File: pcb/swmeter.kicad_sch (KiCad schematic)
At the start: 16 parts, among them J0 Conn_01x02_Female, J1 AudioPlug, J2 Conn_Coaxial, J3 Conn_01x03_Female, J4 Conn_01x03_Female, SW1 SW_SPDT, SW2 SW_SPDT, SW3 SW_DIP_x03, U1 LM3914N

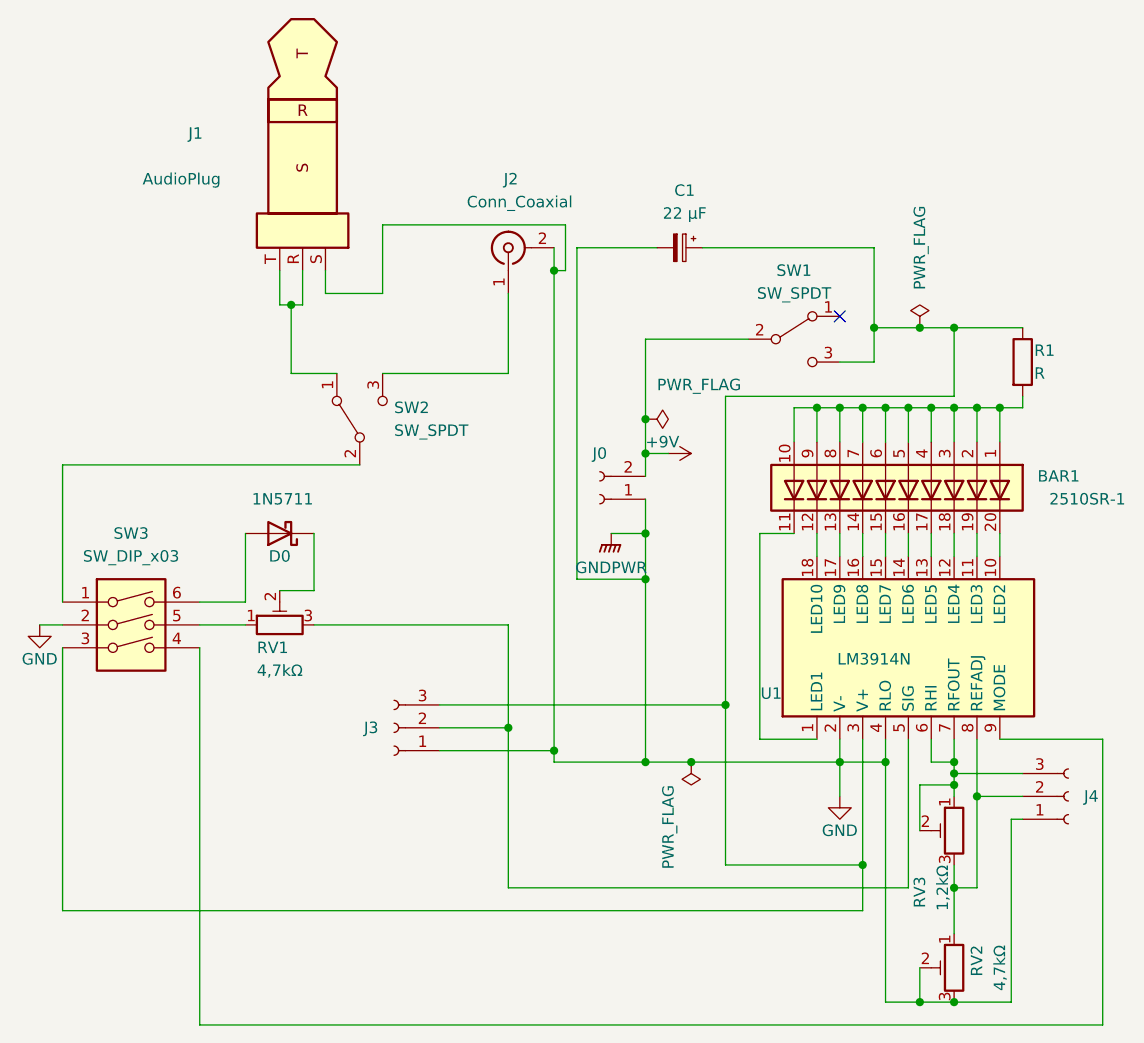
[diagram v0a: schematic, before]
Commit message: add diode for reverse polarity protection
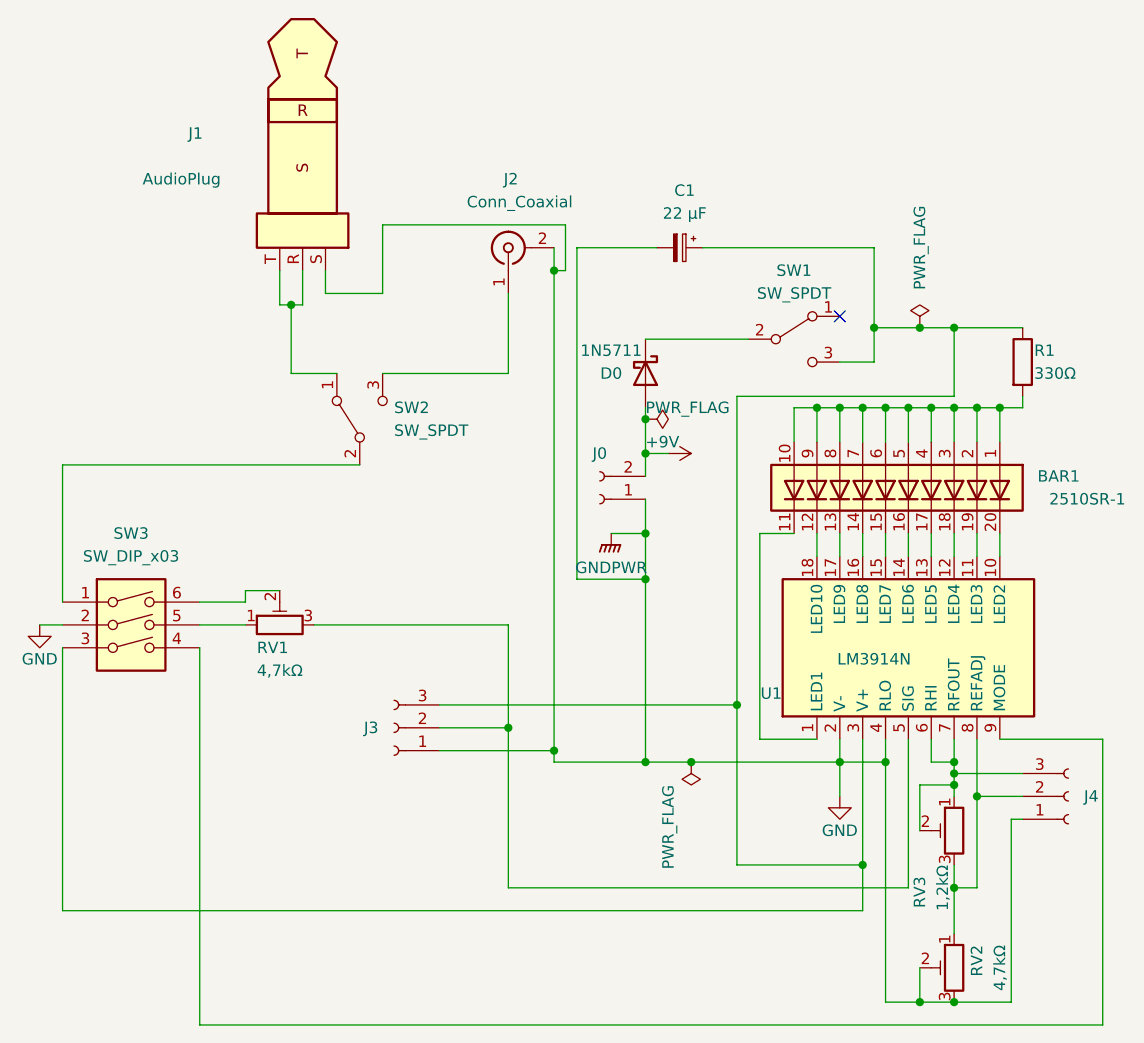
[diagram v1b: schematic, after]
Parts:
- R1: value R -> 330Ω
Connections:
- net +9V: now also D0.2 (A); no longer SW1.2 (B)
- net at SW3.6: now also RV1.2; no longer D0.2 (A)
- net at D0.1 (K): now also SW1.2 (B); no longer RV1.2
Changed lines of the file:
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@@
   (junction (at 250.19 92.71) (diameter 0) (color 0 0 0 0)
   )
+  (junction (at 238.76 125.73) (diameter 0) (color 0 0 0 0)
+  )
   (junction (at 189.23 81.28) (diameter 0) (color 0 0 0 0)
   )
@@
   )
   (junction (at 250.19 132.08) (diameter 0) (color 0 0 0 0)
-  )
-  (junction (at 237.49 125.73) (diameter 0) (color 0 0 0 0)
   )
   (junction (at 265.43 92.71) (diameter 0) (color 0 0 0 0)
@@
     (stroke (width 0) (type default) (color 0 0 0 0))
   )
+  (wire (pts (xy 205.74 125.73) (xy 238.76 125.73))
+    (stroke (width 0) (type default) (color 0 0 0 0))
+  )
   (wire (pts (xy 193.04 80.01) (xy 199.39 80.01))
     (stroke (width 0) (type default) (color 0 0 0 0))
@@
     (stroke (width 0) (type default) (color 0 0 0 0))
   )
+  (wire (pts (xy 184.15 114.3) (xy 184.15 113.03))
+    (stroke (width 0) (type default) (color 0 0 0 0))
+  )
   (wire (pts (xy 219.71 77.47) (xy 218.44 77.47))
     (stroke (width 0) (type default) (color 0 0 0 0))
@@
     (stroke (width 0) (type default) (color 0 0 0 0))
   )
+  (wire (pts (xy 238.76 125.73) (xy 238.76 143.51))
+    (stroke (width 0) (type default) (color 0 0 0 0))
+  )
+  (wire (pts (xy 184.15 113.03) (xy 187.96 113.03))
+    (stroke (width 0) (type default) (color 0 0 0 0))
+  )
   (wire (pts (xy 255.27 158.75) (xy 259.08 158.75))
     (stroke (width 0) (type default) (color 0 0 0 0))
@@
     (stroke (width 0) (type default) (color 0 0 0 0))
   )
-  (wire (pts (xy 228.6 85.09) (xy 228.6 93.98))
-    (stroke (width 0) (type default) (color 0 0 0 0))
-  )
   (wire (pts (xy 205.74 128.27) (xy 213.36 128.27))
     (stroke (width 0) (type default) (color 0 0 0 0))
@@
     (stroke (width 0) (type default) (color 0 0 0 0))
   )
-  (wire (pts (xy 205.74 125.73) (xy 237.49 125.73))
-    (stroke (width 0) (type default) (color 0 0 0 0))
-  )
   (wire (pts (xy 255.27 132.08) (xy 250.19 132.08))
     (stroke (width 0) (type default) (color 0 0 0 0))
@@
     (stroke (width 0) (type default) (color 0 0 0 0))
   )
-  (wire (pts (xy 237.49 143.51) (xy 252.73 143.51))
-    (stroke (width 0) (type default) (color 0 0 0 0))
-  )
   (wire (pts (xy 265.43 135.89) (xy 270.51 135.89))
     (stroke (width 0) (type default) (color 0 0 0 0))
@@
     (stroke (width 0) (type default) (color 0 0 0 0))
   )
+  (wire (pts (xy 228.6 92.71) (xy 228.6 93.98))
+    (stroke (width 0) (type default) (color 0 0 0 0))
+  )
   (wire (pts (xy 259.08 134.62) (xy 262.89 134.62))
     (stroke (width 0) (type default) (color 0 0 0 0))
   )
-  (wire (pts (xy 262.89 91.44) (xy 237.49 91.44))
+  (wire (pts (xy 262.89 91.44) (xy 238.76 91.44))
     (stroke (width 0) (type default) (color 0 0 0 0))
   )
@@
     (stroke (width 0) (type default) (color 0 0 0 0))
   )
-  (wire (pts (xy 237.49 91.44) (xy 237.49 125.73))
+  (wire (pts (xy 238.76 91.44) (xy 238.76 125.73))
     (stroke (width 0) (type default) (color 0 0 0 0))
   )
@@
     (stroke (width 0) (type default) (color 0 0 0 0))
   )
+  (wire (pts (xy 238.76 143.51) (xy 252.73 143.51))
+    (stroke (width 0) (type default) (color 0 0 0 0))
+  )
   (wire (pts (xy 262.89 129.54) (xy 262.89 132.08))
     (stroke (width 0) (type default) (color 0 0 0 0))
@@
     (stroke (width 0) (type default) (color 0 0 0 0))
   )
-  (wire (pts (xy 191.77 106.68) (xy 191.77 113.03))
-    (stroke (width 0) (type default) (color 0 0 0 0))
-  )
   (wire (pts (xy 259.08 83.82) (xy 262.89 83.82))
     (stroke (width 0) (type default) (color 0 0 0 0))
@@
     (stroke (width 0) (type default) (color 0 0 0 0))
   )
-  (wire (pts (xy 237.49 125.73) (xy 237.49 143.51))
-    (stroke (width 0) (type default) (color 0 0 0 0))
-  )
-  (wire (pts (xy 184.15 114.3) (xy 184.15 106.68))
-    (stroke (width 0) (type default) (color 0 0 0 0))
-  )
   (wire (pts (xy 252.73 129.54) (xy 252.73 143.51))
     (stroke (width 0) (type default) (color 0 0 0 0))
@@
   )
   (wire (pts (xy 190.5 77.47) (xy 190.5 81.28))
-    (stroke (width 0) (type default) (color 0 0 0 0))
-  )
-  (wire (pts (xy 191.77 113.03) (xy 187.96 113.03))
     (stroke (width 0) (type default) (color 0 0 0 0))
   )
@@
       (effects (font (size 1.27 1.27)) (justify left))
     )
-    (property "Value" "R" (id 1) (at 271.78 88.9 0)
+    (property "Value" "330Ω" (id 1) (at 271.78 88.9 0)
       (effects (font (size 1.27 1.27)) (justify left))
     )
@@
     (pin "3")
   )
-  (symbol (lib_id "Diode:1N5711") (at 187.96 106.68 180) (unit 1)
-    (in_bom yes) (on_board yes)
-    (property "Reference" "D0" (id 0) (at 187.96 109.22 0))
-    (property "Value" "1N5711" (id 1) (at 188.2775 102.87 0))
-    (property "Footprint" "Diode_THT:D_DO-35_SOD27_P7.62mm_Horizontal" (id 2) (at 187.96 102.235 0)
-      (effects (font (size 1.27 1.27)) hide)
-    )
-    (property "Datasheet" "https://www.microsemi.com/document-portal/doc_download/8865-lds-0040-datasheet" (id 3) (at 187.96 106.68 0)
+  (symbol (lib_id "Diode:1N5711") (at 228.6 88.9 270) (unit 1)
+    (in_bom yes) (on_board yes)
+    (property "Reference" "D0" (id 0) (at 224.79 88.9 90))
+    (property "Value" "1N5711" (id 1) (at 224.79 86.36 90))
+    (property "Footprint" "Diode_THT:D_DO-35_SOD27_P7.62mm_Horizontal" (id 2) (at 224.155 88.9 0)
+      (effects (font (size 1.27 1.27)) hide)
+    )
+    (property "Datasheet" "https://www.microsemi.com/document-portal/doc_download/8865-lds-0040-datasheet" (id 3) (at 228.6 88.9 0)
       (effects (font (size 1.27 1.27)) hide)
     )
@@
       (effects (font (size 1.27 1.27)) hide)
     )
-    (property "Value" "PWR_FLAG" (id 1) (at 229.87 90.17 90)
+    (property "Value" "PWR_FLAG" (id 1) (at 228.6 92.71 90)
       (effects (font (size 1.27 1.27)) (justify left))
     )
@@
       (reference "C1") (unit 1) (value "22 µF") (footprint "Capacitor_THT:CP_Radial_D4.0mm_P2.00mm")
     )
-    (path "/a991215c-d7f8-4d74-b4fb-3a6d0eed12fe"
+    (path "/95568ddf-be8c-46db-99de-cfd2b3a0cf9e"
       (reference "D0") (unit 1) (value "1N5711") (footprint "Diode_THT:D_DO-35_SOD27_P7.62mm_Horizontal")
     )
@@
     )
     (path "/3cca3325-8383-49bc-ad4e-57e30365dacd"
-      (reference "R1") (unit 1) (value "R") (footprint "Resistor_THT:R_Axial_DIN0207_L6.3mm_D2.5mm_P7.62mm_Horizontal")
+      (reference "R1") (unit 1) (value "330Ω") (footprint "Resistor_THT:R_Axial_DIN0207_L6.3mm_D2.5mm_P7.62mm_Horizontal")
     )
     (path "/507fff23-5011-43fc-b0be-f48a3c1431a5"
